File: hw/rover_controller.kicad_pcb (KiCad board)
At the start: 2 copper layers, 2 parts, among them U1 ESP32, U2 LSM6DSMTR

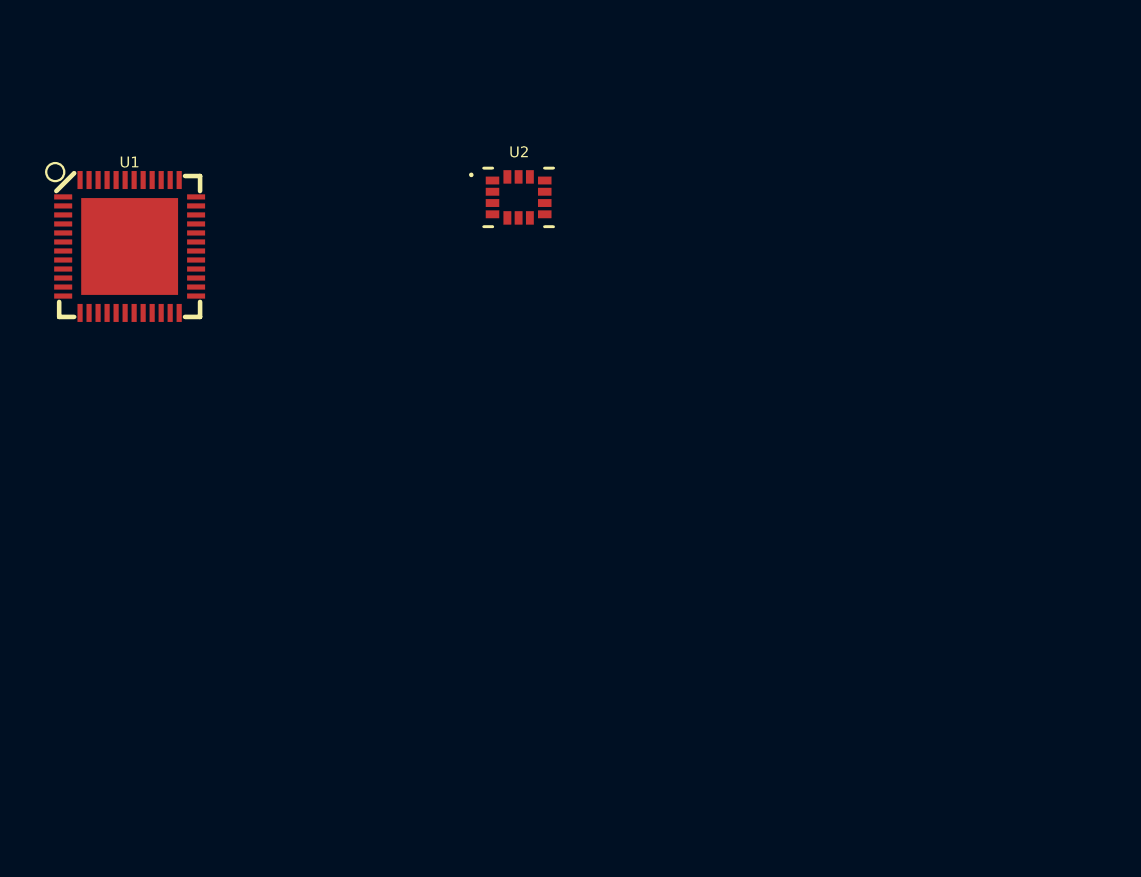
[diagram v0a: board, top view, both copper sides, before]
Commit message: Updated schematics and footprints to use default shared libraries. Updated general schematic
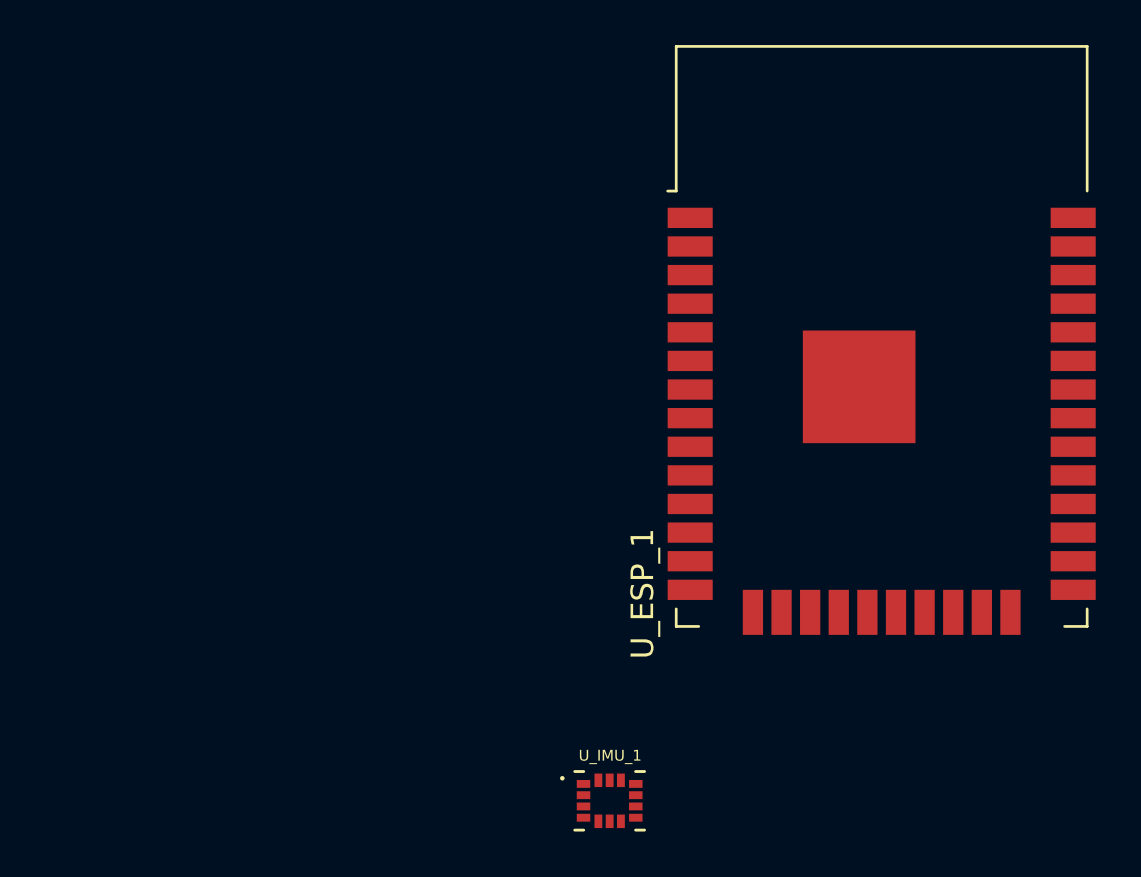
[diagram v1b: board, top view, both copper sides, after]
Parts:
- removed U1: ESP32, footprints:ESP32-WROOM-32D
- removed U2: LSM6DSMTR, footprints:LSM6DSMTR
- added U_ESP_1: ESP32-WROOM-32D, RF_Module:ESP32-WROOM-32, F.Cu at (162.4, 78.4)
- added U_IMU_1: LSM6DSMTR, footprints:LSM6DSMTR, F.Cu at (150.3, 96.0)
